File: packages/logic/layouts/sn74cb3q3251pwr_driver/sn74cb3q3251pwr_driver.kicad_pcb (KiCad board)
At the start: 2 copper layers, 2 parts

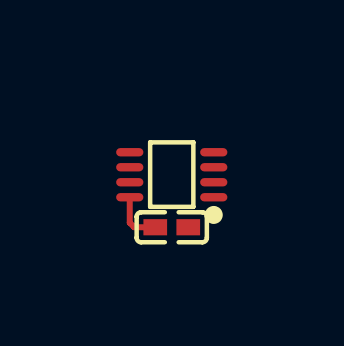
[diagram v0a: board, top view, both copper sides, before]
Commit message: Cleaning-up and updating to latest standards (#23)
* Update packages:

- add required flag
- package > driver method
- cleaning up
- aligning packages

* Rebuild all
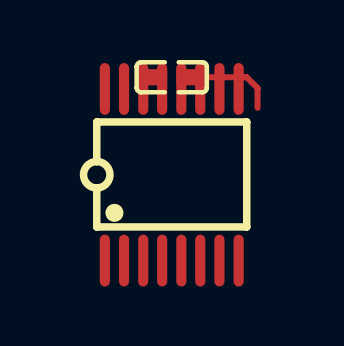
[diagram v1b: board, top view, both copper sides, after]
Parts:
- U1: footprint atopile:VSSOP-8_L2.3-W2.0-P0.50-LS3.1-BR-069dfb -> atopile:TSSOP-16_L5.0-W4.4-P0.64-LS6.4-BL-0862a7
- moved C1 5.00 mm to (0.00, -3.25), turned to 180 degrees
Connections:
- net line renamed a
- net line-1 renamed oe
- net line-2 renamed b[3]
- net line-3 renamed net
- net line-4 renamed b[2]
- net line-5 renamed b[1]
- C1 pad 1: hv -> vcc
- U1 pad 4: gnd -> b[0]
- U1 pad 8: hv -> gnd
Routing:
- net (no net): track 0.00 -> 3.12 mm
- net hv: track 1.76 -> 0.00 mm

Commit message: Fix missing images (#24)
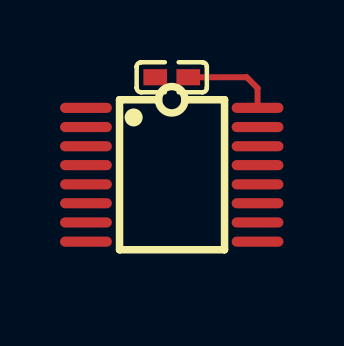
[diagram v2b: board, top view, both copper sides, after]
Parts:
- turned U1 to -90 degrees
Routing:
- net vcc: track 0.00 -> 3.12 mm
- net (no net): track 3.12 -> 0.00 mm

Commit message: Update packages to ato v0.9.x (#36)
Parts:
- C1: footprint atopile:C0402-b3ef17 -> Samsung_Electro_Mechanics_CL05B104KO5NNNC:C0402
- U1: footprint atopile:TSSOP-16_L5.0-W4.4-P0.64-LS6.4-BL-0862a7 -> Texas_Instruments_SN74CB3Q3251PWR:TSSOP-16_L5.0-W4.4-P0.64-LS6.4-BL
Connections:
- net oe renamed nOE
- net s0 renamed S0
- net s1 renamed S1
- net s2 renamed S2
- net vcc renamed VCC
